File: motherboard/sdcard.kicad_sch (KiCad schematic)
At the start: 9 parts, among them J14 Micro_SD_Card_Det1, U18 TPD4EUSB30, U19 TPD4EUSB30

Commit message: linked all footprints
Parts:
- J14: footprint (none) -> microSD_Card:TF-SMD_TF-CARD-H1.8
- R57, R58, R59, R60, R61, R62: footprint (none) -> Resistor_SMD:R_0402_1005Metric
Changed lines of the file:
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@@
 			)
 		)
-		(property "Footprint" ""
+		(property "Footprint" "Resistor_SMD:R_0402_1005Metric"
 			(at 105.41 92.71 0)
 			(effects
@@
 			)
 		)
-		(property "Footprint" ""
+		(property "Footprint" "Resistor_SMD:R_0402_1005Metric"
 			(at 110.49 90.17 0)
 			(effects
@@
 			)
 		)
-		(property "Footprint" ""
+		(property "Footprint" "Resistor_SMD:R_0402_1005Metric"
 			(at 104.14 113.03 0)
 			(effects
@@
 			)
 		)
-		(property "Footprint" ""
+		(property "Footprint" "microSD_Card:TF-SMD_TF-CARD-H1.8"
 			(at 194.31 82.55 0)
 			(effects
@@
 			)
 		)
-		(property "Footprint" ""
+		(property "Footprint" "Resistor_SMD:R_0402_1005Metric"
 			(at 99.06 107.95 0)
 			(effects
@@
 			)
 		)
-		(property "Footprint" ""
+		(property "Footprint" "Resistor_SMD:R_0402_1005Metric"
 			(at 104.14 105.41 0)
 			(effects
@@
 			)
 		)
-		(property "Footprint" ""
+		(property "Footprint" "Resistor_SMD:R_0402_1005Metric"
 			(at 100.33 95.25 0)
 			(effects

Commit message: initial motherboard layout!
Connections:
- net CMD: now also U18.2 (D1-), U18.9 (NC); no longer U18.4 (D2+)
- net D0: now also U19.4 (D2+), U19.7 (NC); no longer U19.1 (D1+)
- net D1: now also U19.9 (NC)
- net D2: now also U18.5 (D2-), U18.6 (NC); no longer U18.1 (D1+)
- net D3: now also U18.4 (D2+), U18.7 (NC); no longer U18.2 (D1-)
- net DET: now also U19.1 (D1+), U19.10 (NC); no longer U19.4 (D2+)
- net SD_CLK: now also U19.5 (D2-), U19.6 (NC); no longer U18.5 (D2-)
- net VCC3V3_SD_S0: now also U18.1 (D1+), U18.10 (NC); no longer U19.5 (D2-)

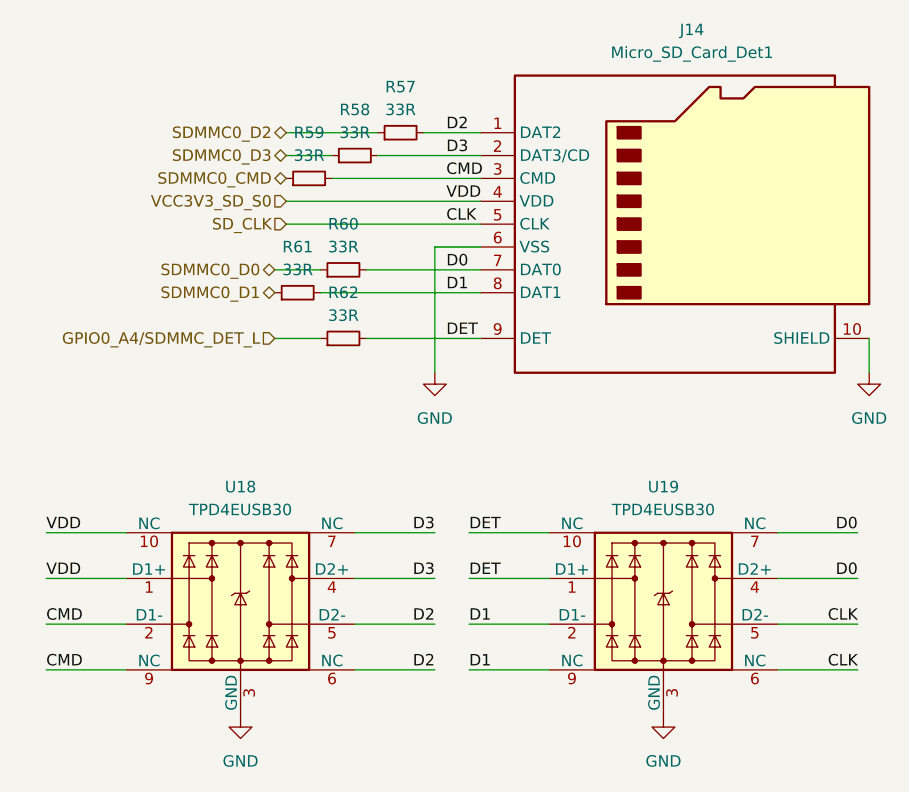
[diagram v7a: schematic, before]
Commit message: placement roughly halfway done
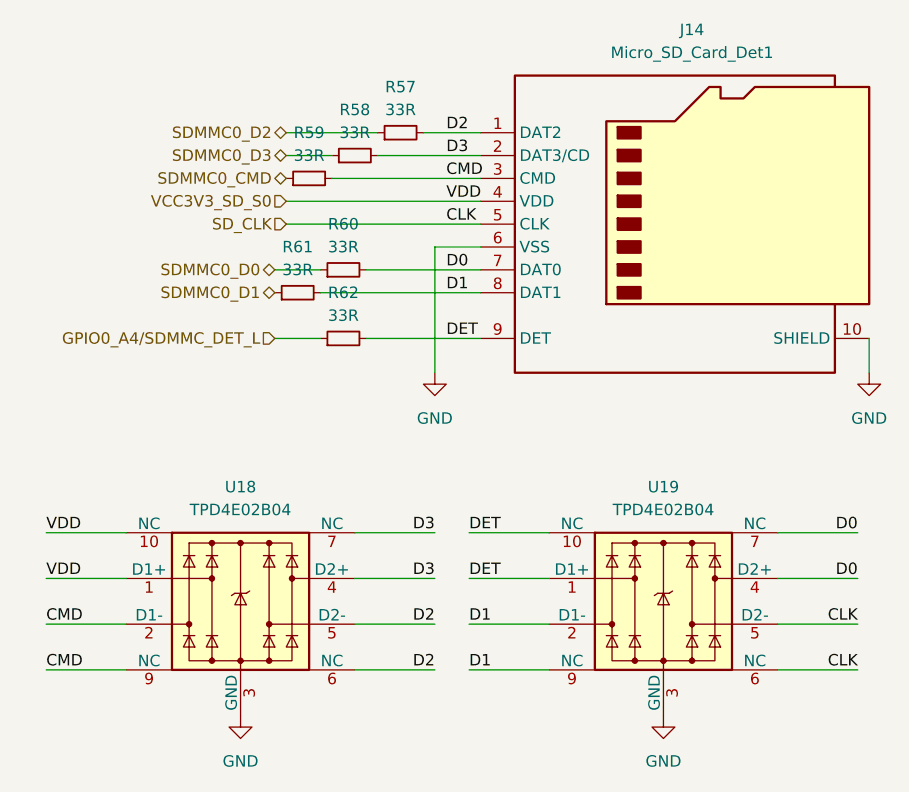
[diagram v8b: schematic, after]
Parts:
- U18, U19: value TPD4EUSB30 -> TPD4E02B04
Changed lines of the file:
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@@
 			)
 		)
-		(property "Value" "TPD4EUSB30"
+		(property "Value" "TPD4E02B04"
 			(at 139.7 132.08 0)
 			(effects
@@
 			)
 		)
-		(property "Value" "TPD4EUSB30"
+		(property "Value" "TPD4E02B04"
 			(at 92.71 132.08 0)
 			(effects
